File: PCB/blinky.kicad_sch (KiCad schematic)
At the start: 1 part, among them U1 7555

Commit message: Create schematic
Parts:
- added BT1: CR2032, symbol Device:Battery_Cell
- added C1: 1U, symbol Device:C
- added D1: LED, symbol Device:LED
- added R1, R3: 1K, symbol Device:R
- added R2: 470K, symbol Device:R
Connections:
- net GND: now reaches U1.1 (GND)
- net GND: now also BT1.2 (-), C1.2, D1.1 (K)
- net at U1.2 (~TRIG~): now also U1.6 (THR), C1.1, R2.2
- net at U1.3 (OUT): now also R3.1
- net at U1.4 (~RST~): now also U1.8 (VDD), BT1.1 (+), R1.1
- net at U1.7 (DIS): now also R1.2, R2.1
- new net: D1.2 (A), R3.2
- no-connect marks 0 -> 1
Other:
- moved on the sheet: U1

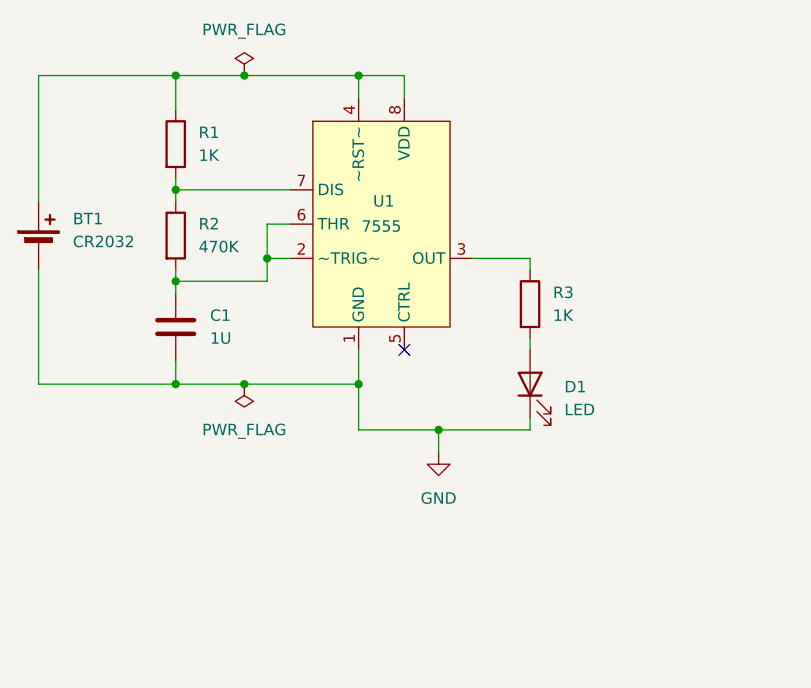
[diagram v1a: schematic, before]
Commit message: Create and update footprints
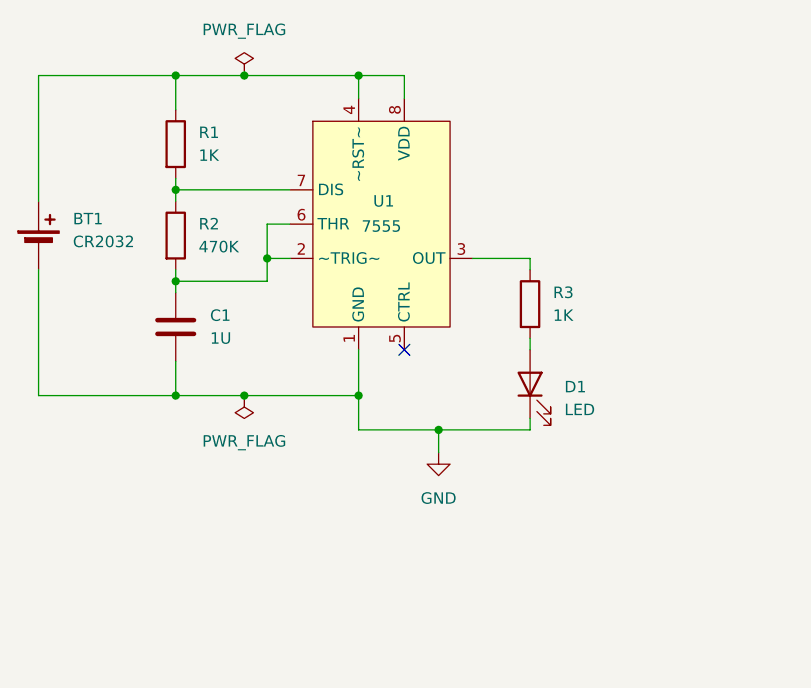
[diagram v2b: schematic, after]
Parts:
- BT1: footprint (none) -> Blinky:S8211-46R
- C1: footprint (none) -> Capacitor_SMD:C_0805_2012Metric_Pad1.18x1.45mm_HandSolder
- D1: footprint (none) -> LED_SMD:LED_0805_2012Metric_Pad1.15x1.40mm_HandSolder
- R1, R2, R3: footprint (none) -> Resistor_SMD:R_0805_2012Metric_Pad1.20x1.40mm_HandSolder
- U1: footprint (none) -> Package_SO:SOIC-8_3.9x4.9mm_P1.27mm
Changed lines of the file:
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@@
+	)
+	(junction
+		(at 99.06 76.2)
+		(diameter 0)
+		(color 0 0 0 0)
+	)
+	(junction
+		(at 91.44 76.2)
+		(diameter 0)
+		(color 0 0 0 0)
 	)
 	(junction
@@
 	)
 	(junction
-		(at 99.06 74.93)
-		(diameter 0)
-		(color 0 0 0 0)
-	)
-	(junction
 		(at 91.44 63.5)
-		(diameter 0)
-		(color 0 0 0 0)
-	)
-	(junction
-		(at 91.44 74.93)
 		(diameter 0)
 		(color 0 0 0 0)
@@
 	)
 	(junction
-		(at 111.76 74.93)
+		(at 111.76 76.2)
 		(diameter 0)
 		(color 0 0 0 0)
@@
 	(wire
 		(pts
-			(xy 111.76 74.93) (xy 111.76 80.01)
-		)
-		(stroke
-			(width 0)
-			(type default)
-		)
-	)
-	(wire
-		(pts
 			(xy 91.44 62.23) (xy 91.44 63.5)
 		)
@@
 	(wire
 		(pts
-			(xy 111.76 71.12) (xy 111.76 74.93)
-		)
-		(stroke
-			(width 0)
-			(type default)
-		)
-	)
-	(wire
-		(pts
-			(xy 99.06 74.93) (xy 111.76 74.93)
+			(xy 99.06 76.2) (xy 111.76 76.2)
 		)
 		(stroke
@@
 	(wire
 		(pts
+			(xy 111.76 71.12) (xy 111.76 76.2)
+		)
+		(stroke
+			(width 0)
+			(type default)
+		)
+	)
+	(wire
+		(pts
 			(xy 99.06 40.64) (xy 111.76 40.64)
 		)
@@
 	(wire
 		(pts
-			(xy 91.44 74.93) (xy 99.06 74.93)
+			(xy 91.44 72.39) (xy 91.44 76.2)
+		)
+		(stroke
+			(width 0)
+			(type default)
+		)
+	)
+	(wire
+		(pts
+			(xy 91.44 76.2) (xy 99.06 76.2)
 		)
 		(stroke
@@
 	(wire
 		(pts
+			(xy 111.76 76.2) (xy 111.76 80.01)
+		)
+		(stroke
+			(width 0)
+			(type default)
+		)
+	)
+	(wire
+		(pts
 			(xy 101.6 60.96) (xy 101.6 63.5)
 		)
@@
 	(wire
 		(pts
-			(xy 91.44 72.39) (xy 91.44 74.93)
-		)
-		(stroke
-			(width 0)
-			(type default)
-		)
-	)
-	(wire
-		(pts
 			(xy 130.81 71.12) (xy 130.81 69.85)
 		)
@@
 	(wire
 		(pts
-			(xy 76.2 74.93) (xy 91.44 74.93)
-		)
-		(stroke
-			(width 0)
-			(type default)
-		)
-	)
-	(wire
-		(pts
-			(xy 76.2 74.93) (xy 76.2 62.23)
+			(xy 76.2 76.2) (xy 91.44 76.2)
+		)
+		(stroke
+			(width 0)
+			(type default)
+		)
+	)
+	(wire
+		(pts
+			(xy 76.2 76.2) (xy 76.2 62.23)
 		)
 		(stroke
@@
 			)
 		)
-		(property "Footprint" ""
+		(property "Footprint" "Capacitor_SMD:C_0805_2012Metric_Pad1.18x1.45mm_HandSolder"
 			(at 92.4052 72.39 0)
 			(effects
@@
 			)
 		)
-		(property "Footprint" ""
+		(property "Footprint" "Blinky:S8211-46R"
 			(at 76.2 58.166 90)
 			(effects
@@
 			)
 		)
-		(property "Footprint" ""
+		(property "Footprint" "LED_SMD:LED_0805_2012Metric_Pad1.15x1.40mm_HandSolder"
 			(at 130.81 74.93 0)
 			(effects
@@
 			)
 		)
-		(property "Footprint" ""
+		(property "Footprint" "Resistor_SMD:R_0805_2012Metric_Pad1.20x1.40mm_HandSolder"
 			(at 89.662 48.26 90)
 			(effects
@@
 			)
 		)
-		(property "Footprint" ""
+		(property "Footprint" "Resistor_SMD:R_0805_2012Metric_Pad1.20x1.40mm_HandSolder"
 			(at 89.662 58.42 90)
 			(effects
@@
 			)
 		)
-		(property "Footprint" ""
+		(property "Footprint" "Resistor_SMD:R_0805_2012Metric_Pad1.20x1.40mm_HandSolder"
 			(at 129.032 66.04 90)
 			(effects
@@
 	(symbol
 		(lib_id "power:PWR_FLAG")
-		(at 99.06 74.93 180)
+		(at 99.06 76.2 180)
 		(unit 1)
 		(exclude_from_sim no)
@@
 		(fields_autoplaced yes)
 		(property "Reference" "#FLG02"
-			(at 99.06 76.835 0)
+			(at 99.06 78.105 0)
 			(effects
 				(font
@@
 		)
 		(property "Value" "PWR_FLAG"
-			(at 99.06 80.01 0)
+			(at 99.06 81.28 0)
 			(effects
 				(font
@@
 		)
 		(property "Footprint" ""
-			(at 99.06 74.93 0)
+			(at 99.06 76.2 0)
 			(effects
 				(font
@@
 		)
 		(property "Datasheet" "~"
-			(at 99.06 74.93 0)
+			(at 99.06 76.2 0)
 			(effects
 				(font
@@
 		)
 		(property "Description" "Special symbol for telling ERC where power comes from"
-			(at 99.06 74.93 0)
+			(at 99.06 76.2 0)
 			(effects
 				(font
@@
 			)
 		)
-		(property "Footprint" ""
+		(property "Footprint" "Package_SO:SOIC-8_3.9x4.9mm_P1.27mm"
 			(at 114.3 53.34 0)
 			(effects
